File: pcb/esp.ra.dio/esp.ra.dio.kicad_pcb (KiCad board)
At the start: 2 copper layers, 75 x 28 mm, 26 parts, among them J1 A, J10 UART, J2 B, J3 C, J4 D, J5 START, J6 SELECT, J7 JOY, J8 USB_B_Micro, J9 BATTERY, SW1 RESET, SW2 POWER, SW3 BOOT, U2 ESP32-C3-WROOM-02, U3 TLV75533PDBV

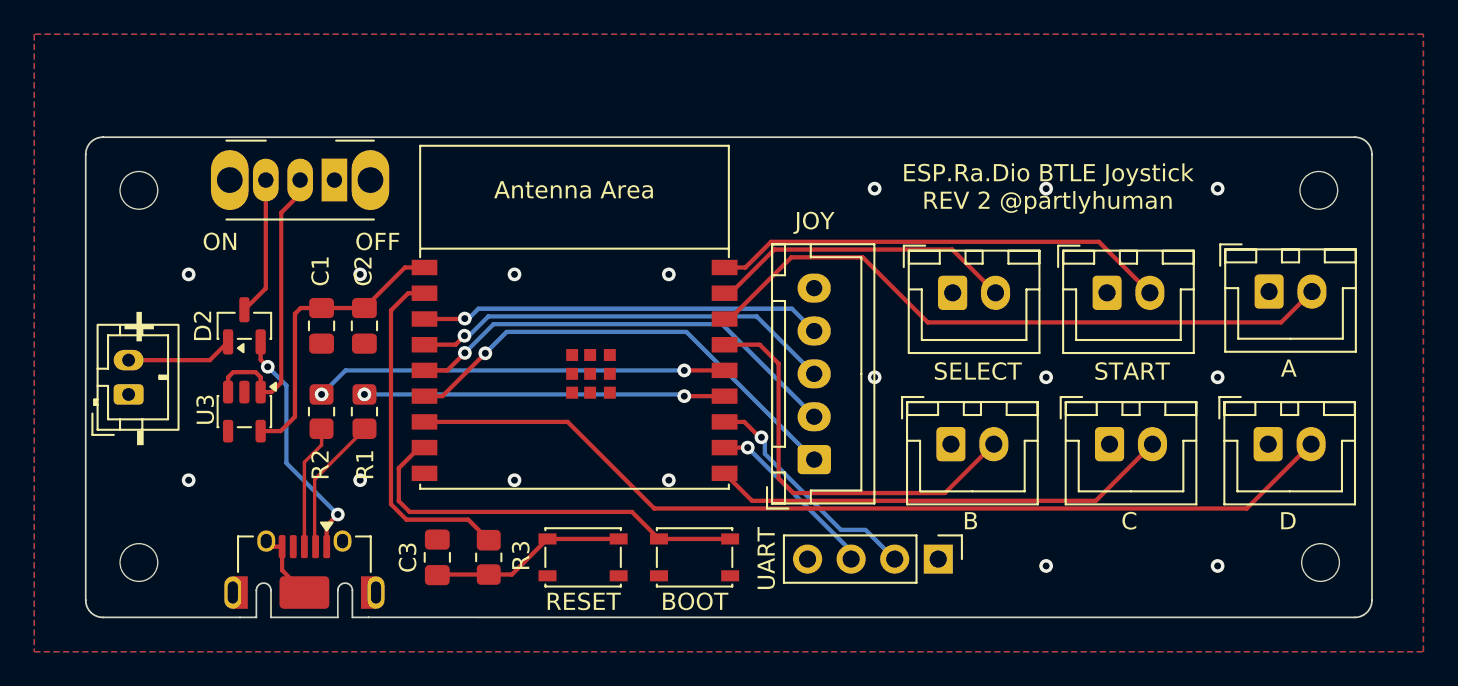
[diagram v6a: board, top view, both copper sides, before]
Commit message: Fix EN needs pullup
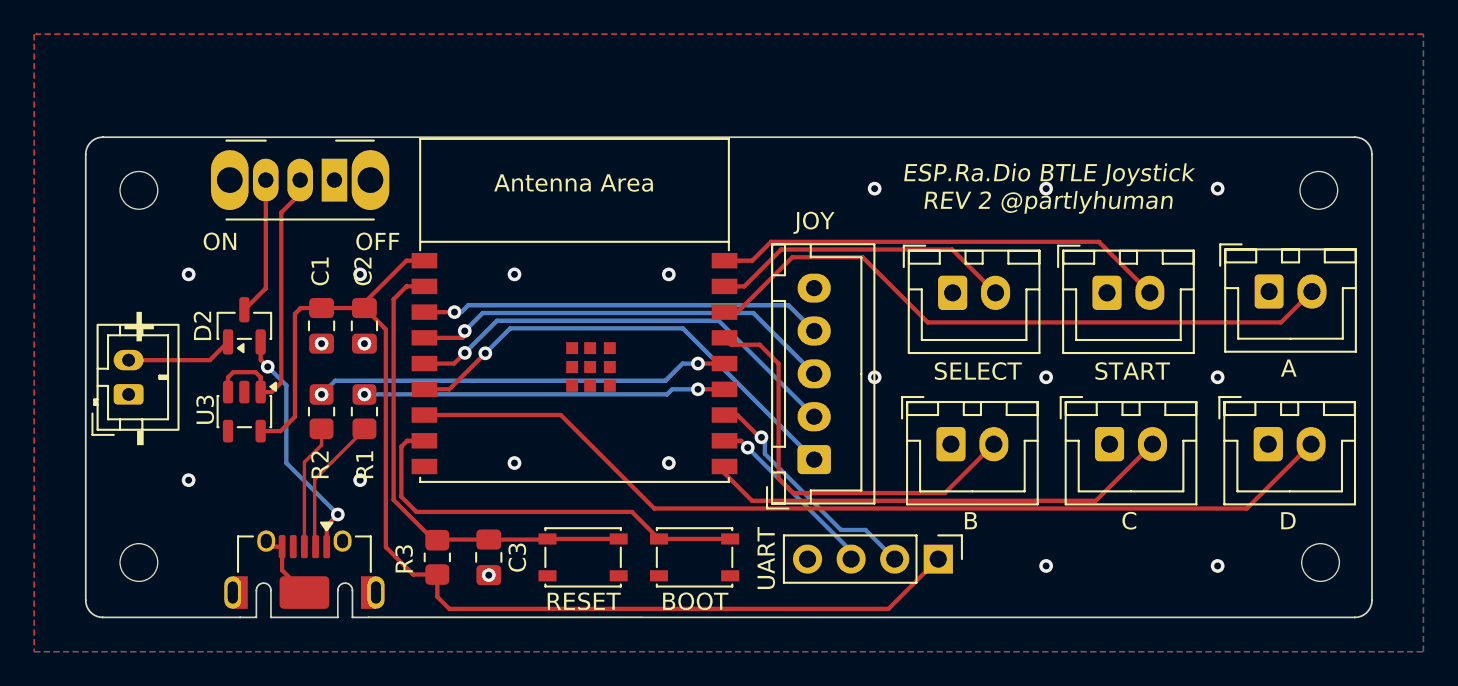
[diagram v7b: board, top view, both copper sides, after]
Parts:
- U2: value ESP32-C3-WROOM-02 -> VCC
- moved C3 3.00 mm to (61.5, 74.5), turned to 90 degrees
- moved R3 3.00 mm to (58.5, 74.5), turned to -90 degrees
- moved U2 0.40 mm to (66.5, 63.1)
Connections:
- C1 pad 1: Net-(U2-3V3) -> VCC
- C2 pad 1: Net-(U2-3V3) -> VCC
- C3 pad 2: Net-(C3-Pad2) -> /EN
- J10 pad 1: /VCC -> VCC
- R3 pad 1: Net-(C3-Pad2) -> /EN
- R3 pad 2: Net-(U2-EN/CHIP_PU) -> VCC
- SW1 pad 1: Net-(C3-Pad2) -> /EN
- U2 pad 1: Net-(U2-3V3) -> VCC
- U2 pad 2: Net-(U2-EN/CHIP_PU) -> /EN
- U3 pad 5: Net-(U2-3V3) -> VCC
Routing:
- net VCC: track 0.00 -> 67.5 mm
- net /EN: track 0.00 -> 27.9 mm
- net Net-(U2-EN/CHIP_PU): track 20.2 -> 0.00 mm
- net Net-(U2-3V3): track 17.0 -> 0.00 mm
- net Net-(C3-Pad2): track 11.5 -> 0.00 mm
- net GND: vias 16 -> 19

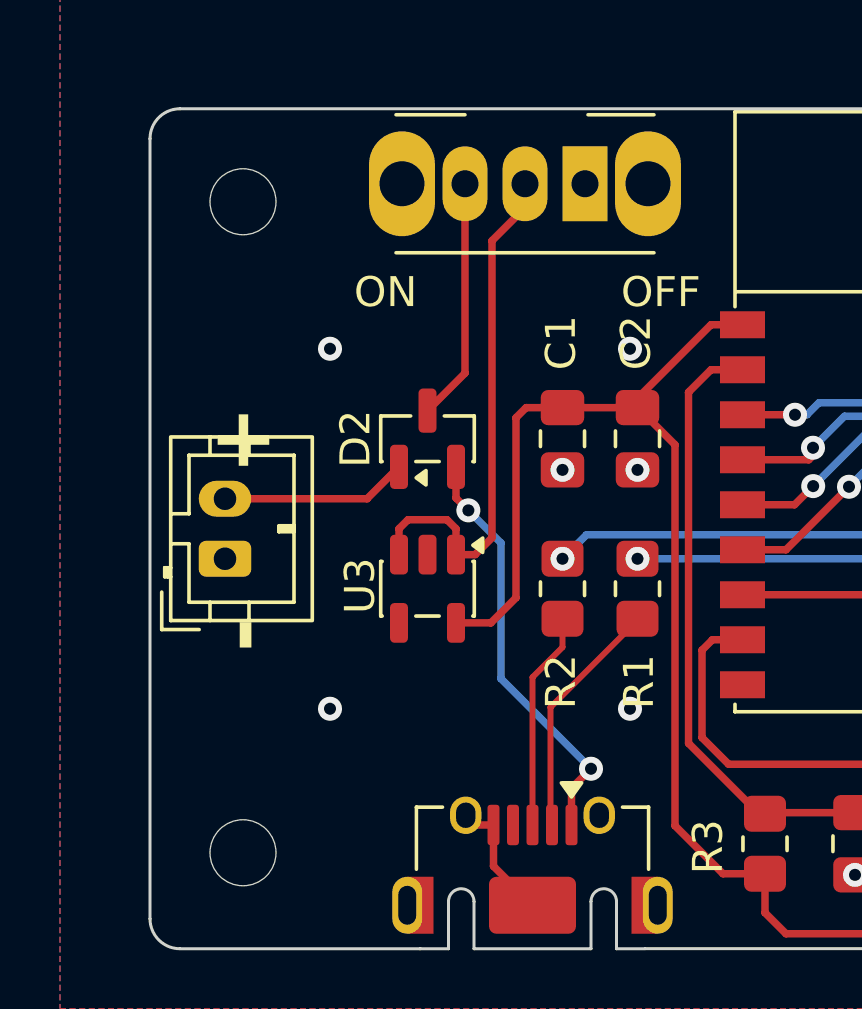
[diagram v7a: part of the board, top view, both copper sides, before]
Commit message: Removes USB power, diode drop would have eaten into battery life too much
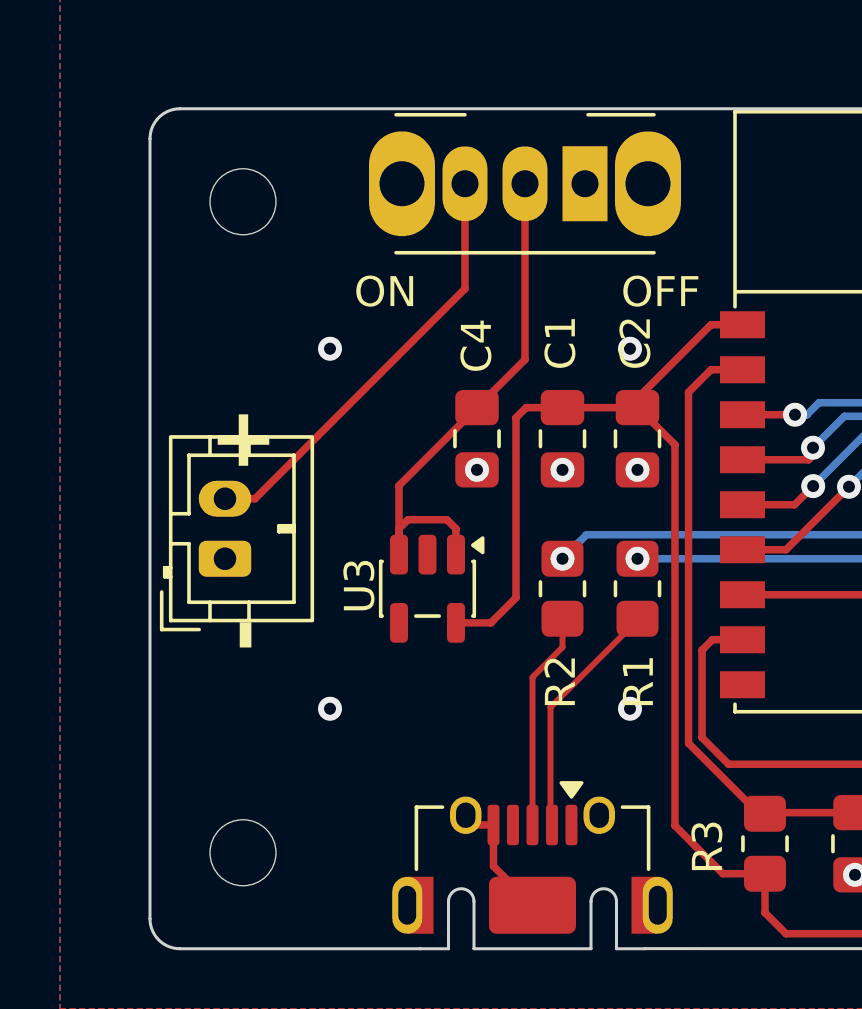
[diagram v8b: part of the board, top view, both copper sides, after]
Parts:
- removed D2: BAT54C, Package_TO_SOT_SMD:SOT-23
- added C4: 10uF, Capacitor_SMD:C_0805_2012Metric_Pad1.18x1.45mm_HandSolder, F.Cu at (48.9, 61.0)
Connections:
- J8 pad 1: /VBUS -> unconnected-(J8-VBUS-Pad1)
- SW2 pad 3: /VBATBUS -> /VBAT
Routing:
- net /VBUS: track 14.1 -> 0.00 mm, vias 2 -> 0
- net /VBAT: track 6.24 -> 14.4 mm
- net /VBATBUS: track 8.08 -> 0.00 mm
- net GND: vias 19 -> 20
